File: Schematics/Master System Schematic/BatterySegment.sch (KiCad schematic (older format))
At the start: 148 parts

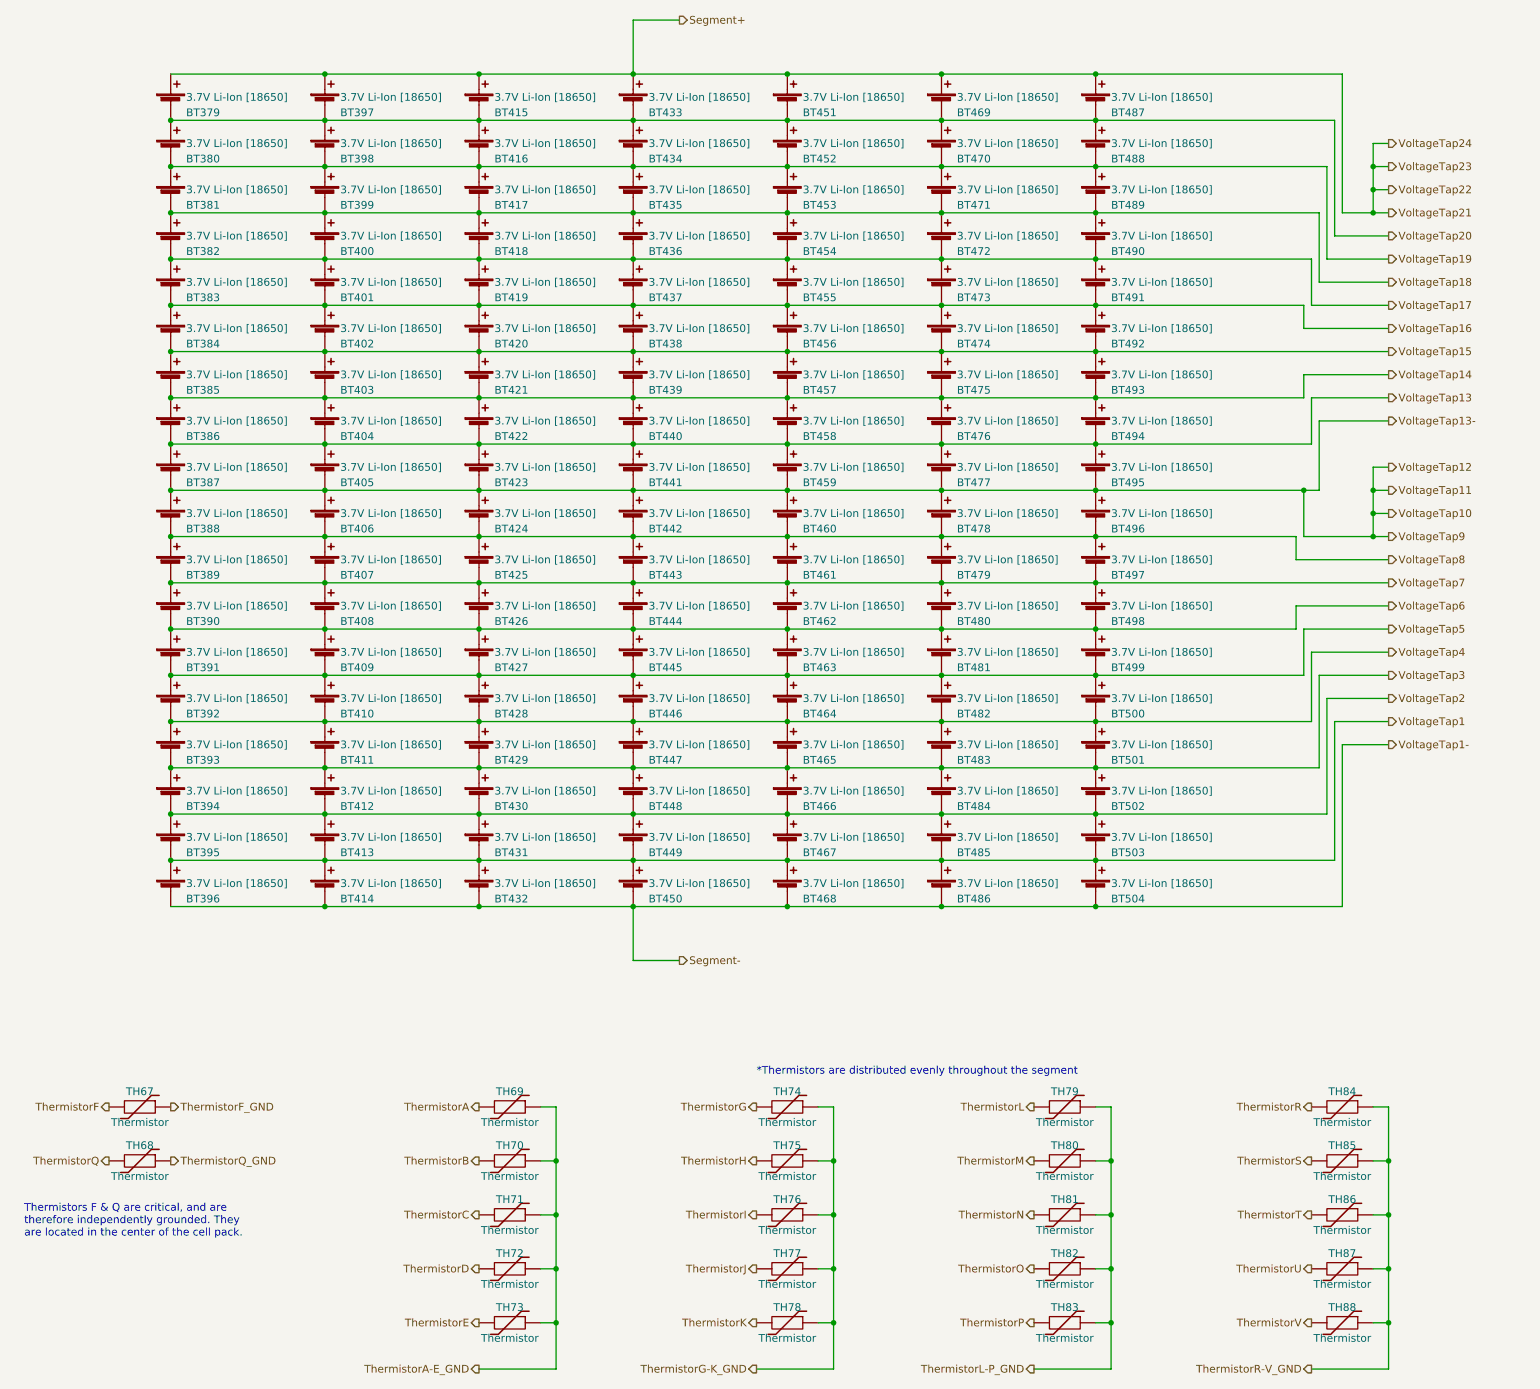
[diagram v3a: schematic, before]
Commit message: Had to refactor all IDs
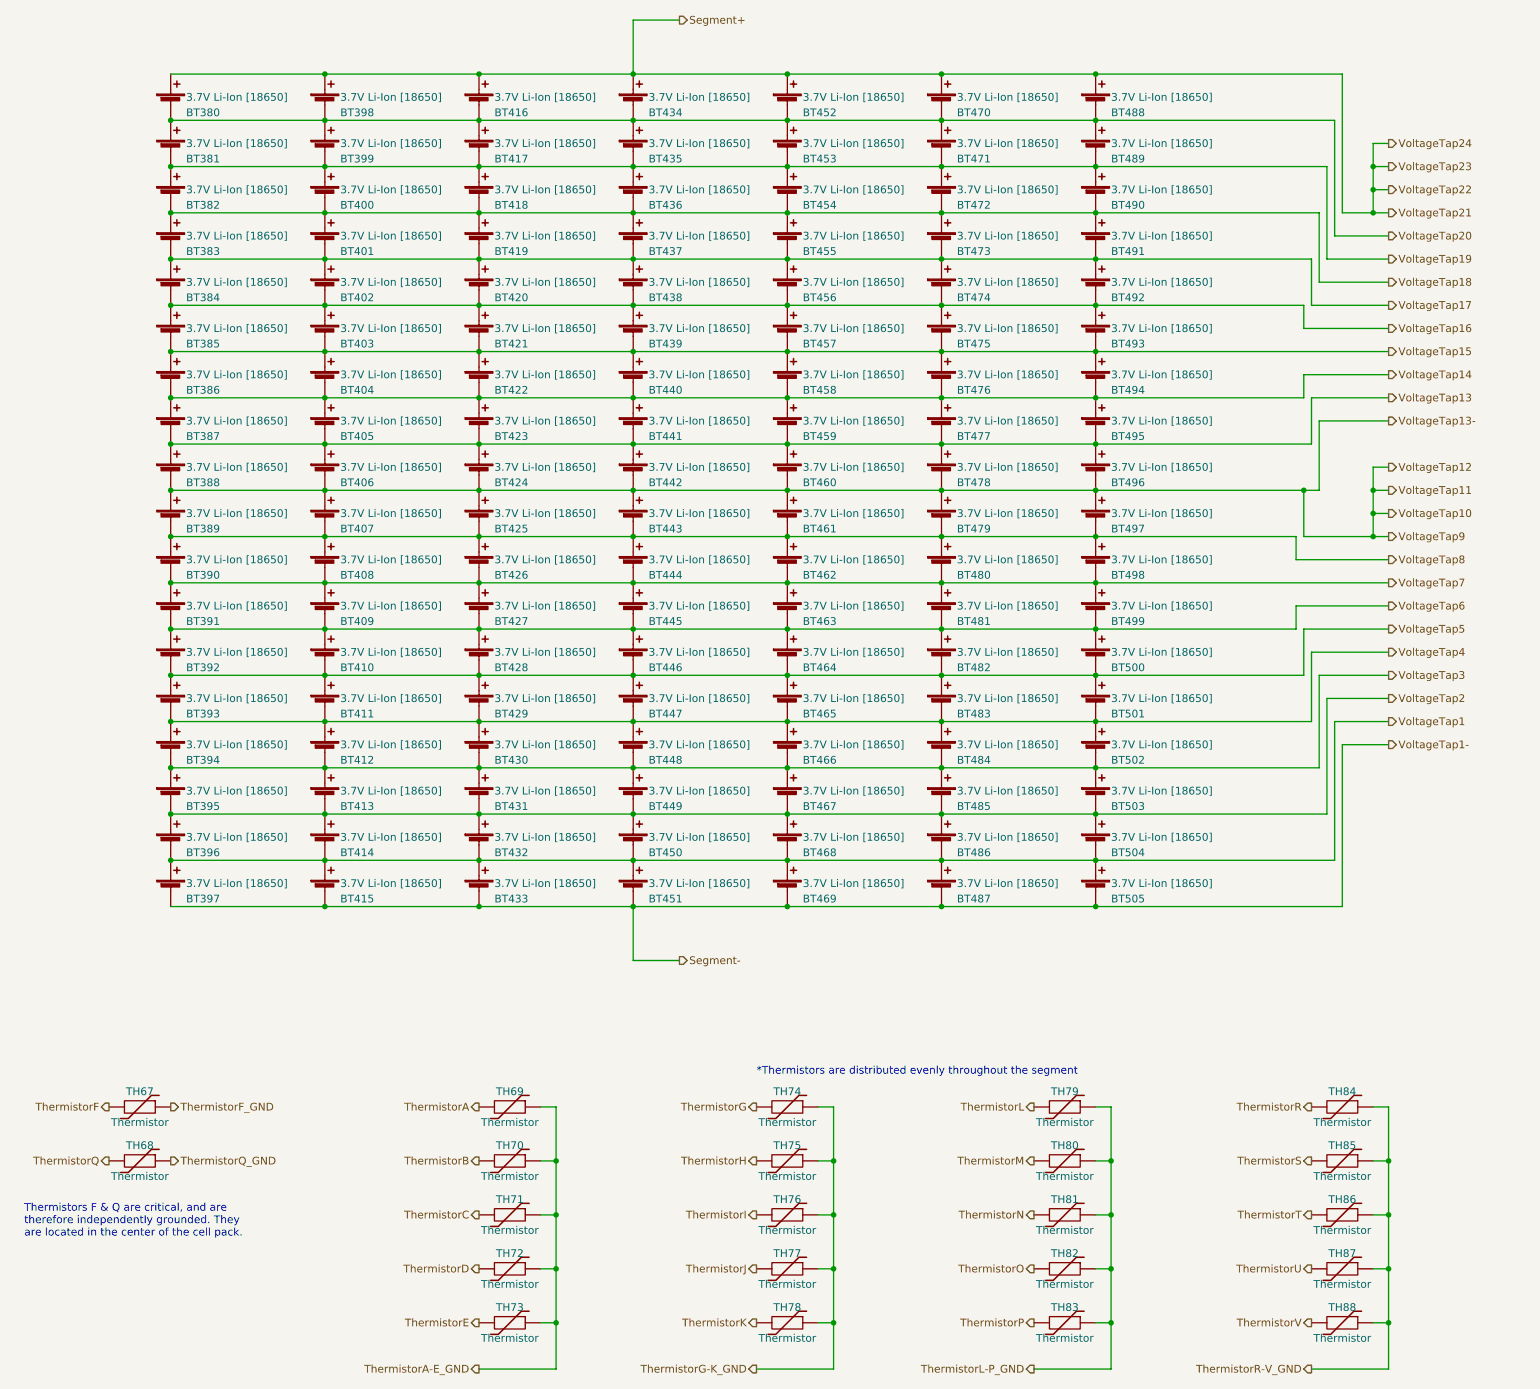
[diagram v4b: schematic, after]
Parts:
- renumbered BT15 to BT10, BT16 to BT11, BT7 to BT110, BT110 to BT111, BT111 to BT112, BT112 to BT113, BT113 to BT114, BT114 to BT115, BT115 to BT116, BT116 to BT117, BT117 to BT118, BT118 to BT119, BT17 to BT12, BT119 to BT120, BT120 to BT121, BT121 to BT122, BT122 to BT123, BT123 to BT124, BT124 to BT125, BT125 to BT126, BT126 to BT127, BT18 to BT13, BT19 to BT14, BT20 to BT15, BT21 to BT16, BT22 to BT17, BT23 to BT18, BT24 to BT19, BT1 to BT2, BT2 to BT20, BT25 to BT21, BT26 to BT22, BT27 to BT23, BT28 to BT24, BT29 to BT25, BT30 to BT26, BT31 to BT27, BT32 to BT28, BT33 to BT29, BT8 to BT3, BT34 to BT30, BT35 to BT31, BT36 to BT32, BT37 to BT33, BT38 to BT34, BT39 to BT35, BT40 to BT36, BT41 to BT37, BT3 to BT38, BT42 to BT39, BT9 to BT4, BT43 to BT40, BT44 to BT41, BT45 to BT42, BT46 to BT43, BT47 to BT44, BT48 to BT45, BT49 to BT46, BT50 to BT47, BT51 to BT48, BT52 to BT49, BT10 to BT5, BT53 to BT50, BT54 to BT51, BT55 to BT52, BT56 to BT53, BT57 to BT54, BT58 to BT55, BT4 to BT56, BT59 to BT57, BT60 to BT58, BT61 to BT59, BT11 to BT6, BT62 to BT60, BT63 to BT61, BT64 to BT62, BT65 to BT63, BT66 to BT64, BT67 to BT65, BT68 to BT66, BT69 to BT67, BT70 to BT68, BT71 to BT69, BT12 to BT7, BT72 to BT70, BT73 to BT71, BT74 to BT72, BT75 to BT73, BT5 to BT74, BT76 to BT75, BT77 to BT76, BT78 to BT77, BT79 to BT78, BT80 to BT79, BT13 to BT8, BT81 to BT80, BT82 to BT81, BT83 to BT82, BT84 to BT83, BT85 to BT84, BT86 to BT85, BT87 to BT86, BT88 to BT87, BT89 to BT88, BT90 to BT89, BT14 to BT9, BT91 to BT90, BT92 to BT91, BT6 to BT92, TH6 to TH1, TH9 to TH10, TH10 to TH11, TH11 to TH12, TH12 to TH13, TH13 to TH14, TH14 to TH15, TH15 to TH16, TH16 to TH17, TH17 to TH2, TH1 to TH3, TH2 to TH4, TH3 to TH5, TH4 to TH6, TH5 to TH7, TH7 to TH8, TH8 to TH9

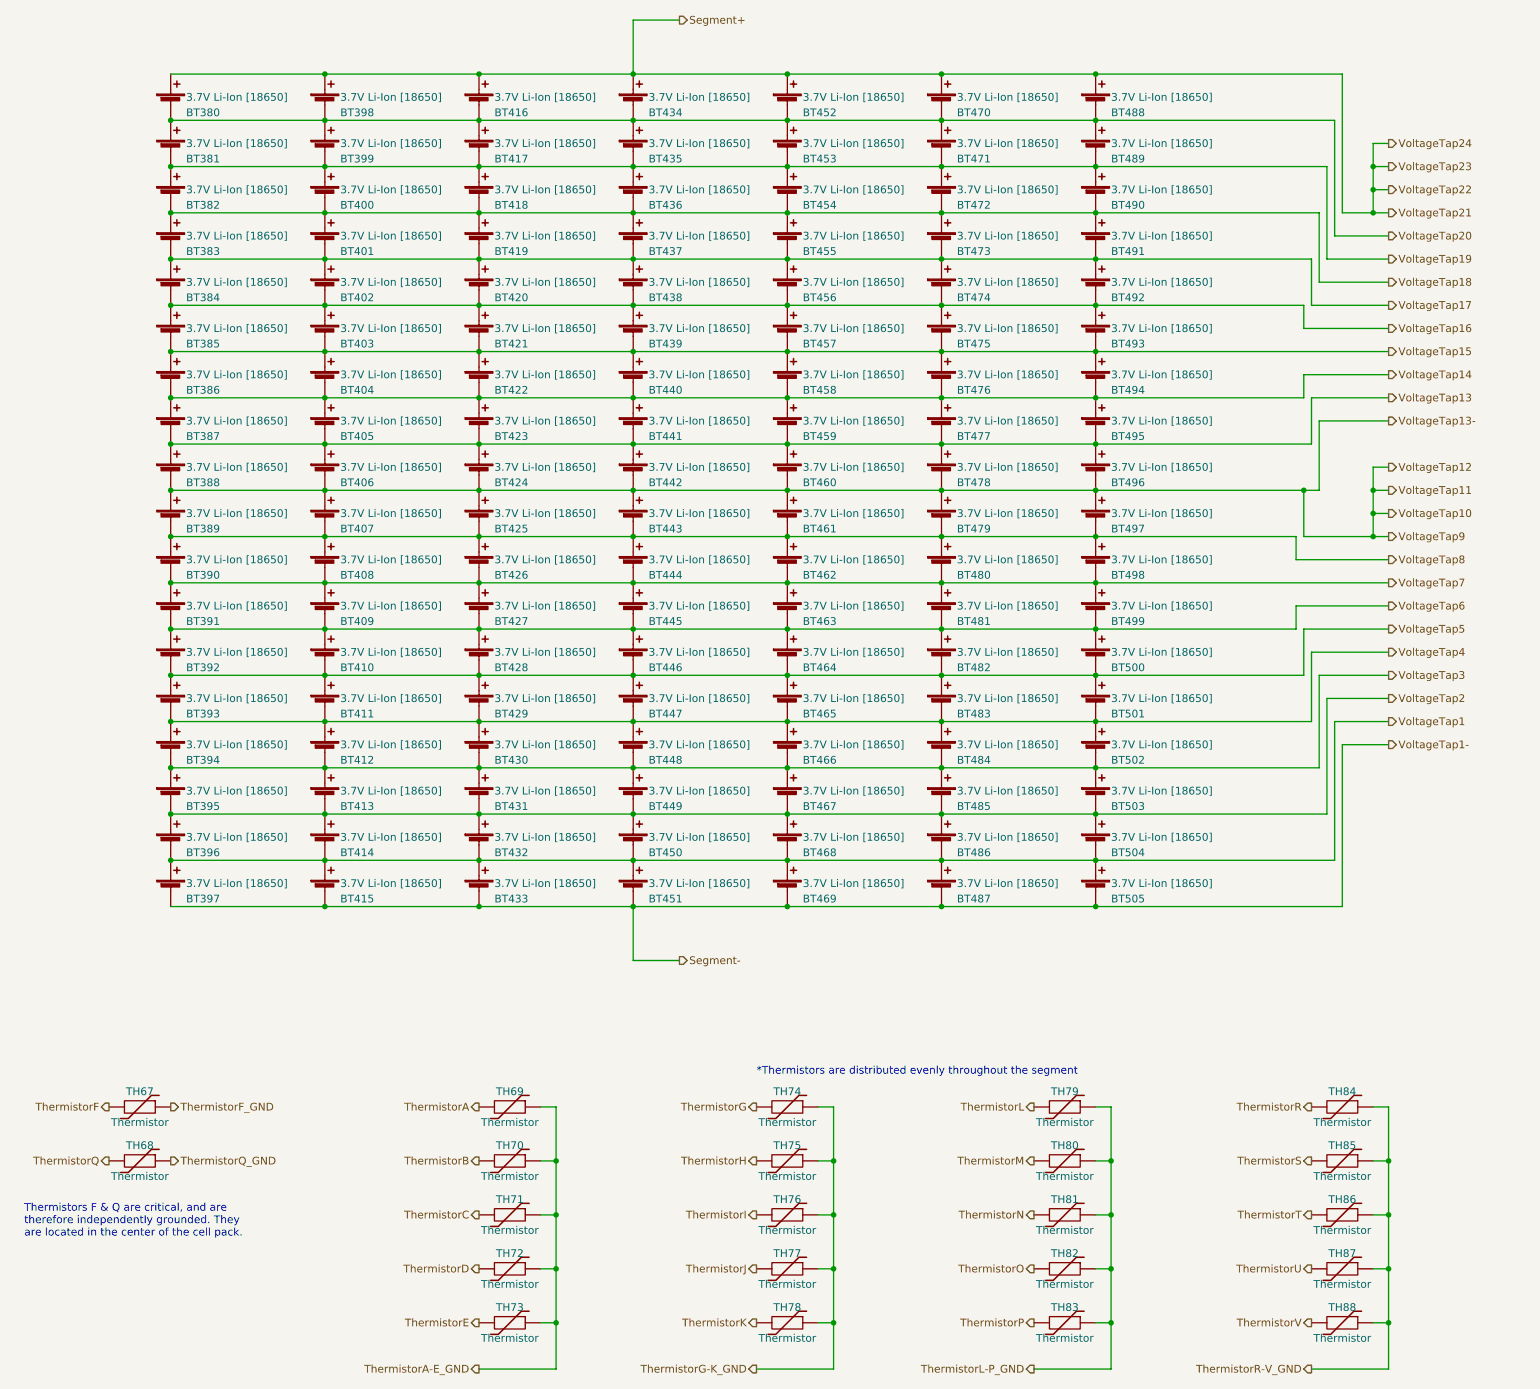
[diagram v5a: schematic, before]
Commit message: Fixed Segment tap wiring
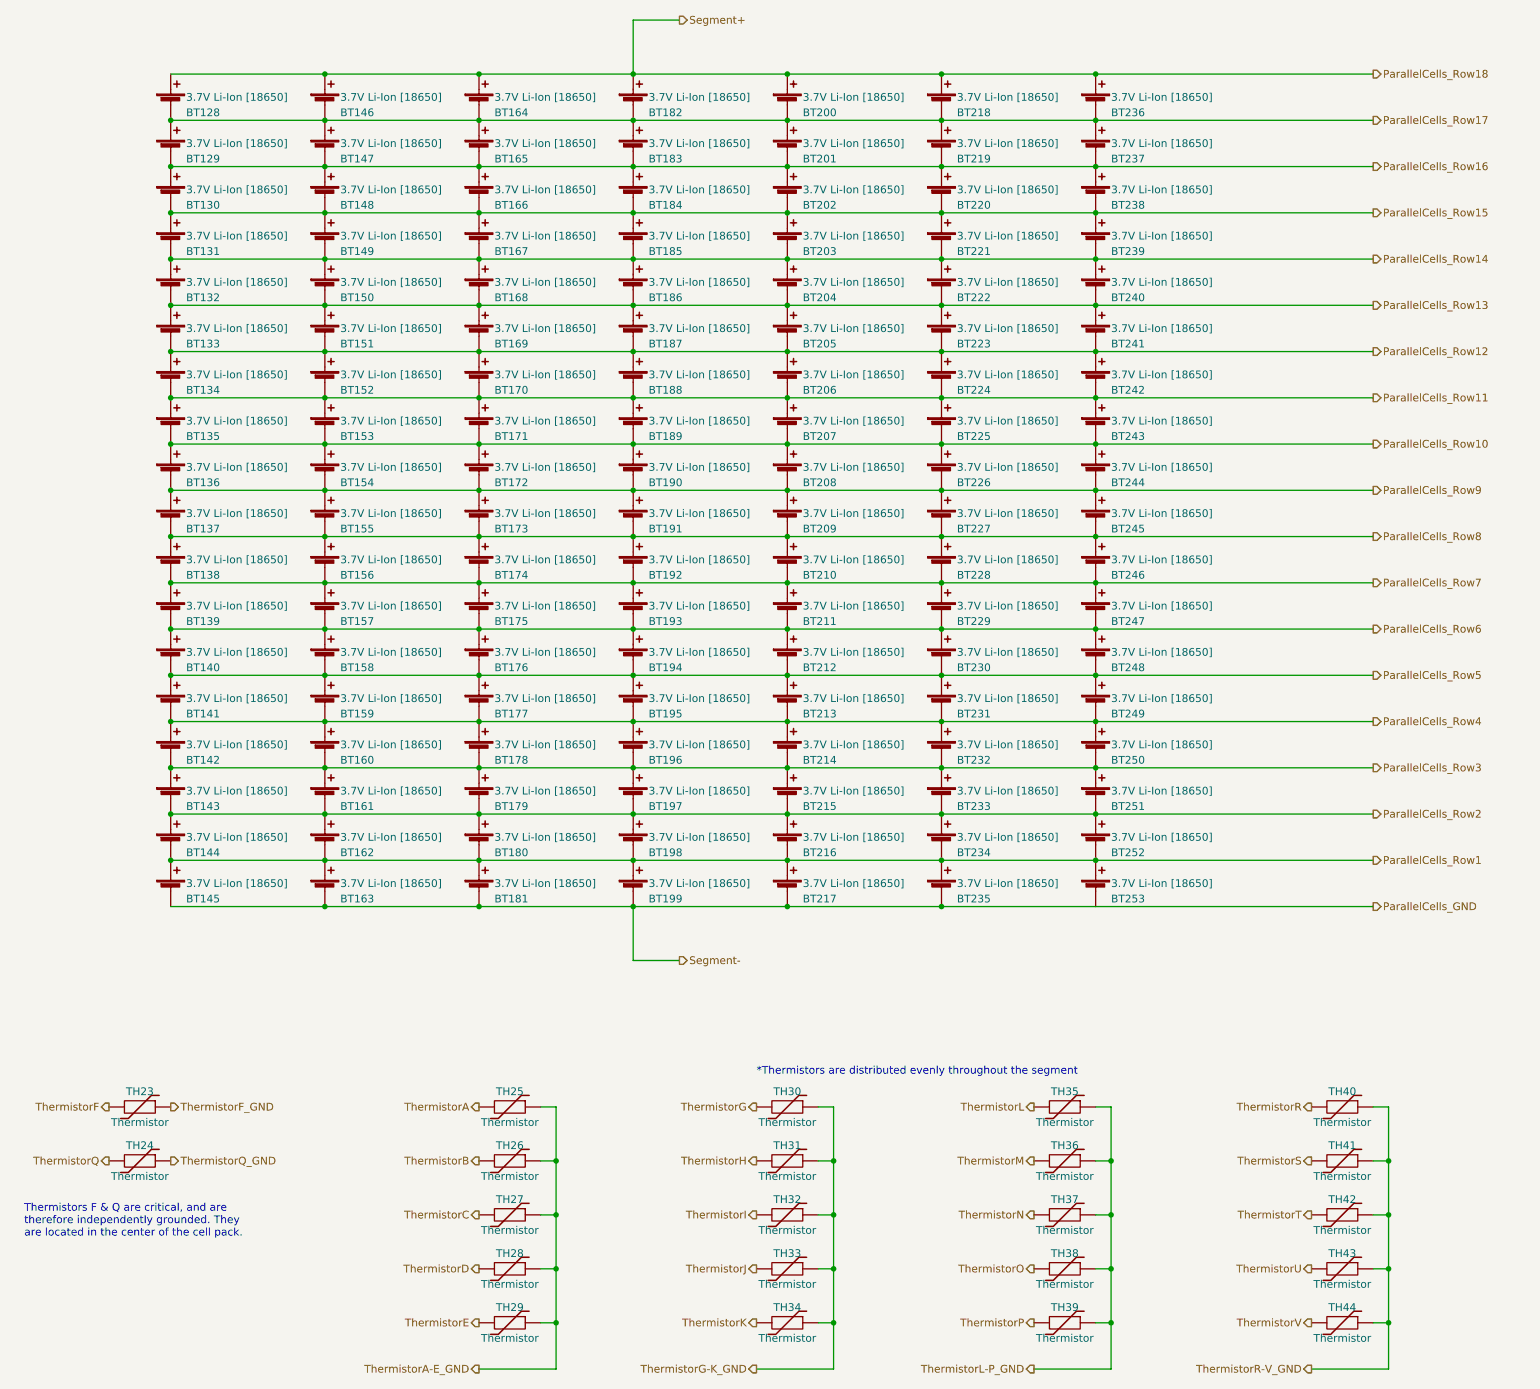
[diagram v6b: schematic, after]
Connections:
- net Segment+ renamed ParallelCells_Row18
- net Segment- renamed ParallelCells_GND
- net VoltageTap1 renamed ParallelCells_Row1
- net VoltageTap10 renamed ParallelCells_Row9
- net VoltageTap13 renamed ParallelCells_Row10
- net VoltageTap14 renamed ParallelCells_Row11
- net VoltageTap15 renamed ParallelCells_Row12
- net VoltageTap16 renamed ParallelCells_Row13
- net VoltageTap17 renamed ParallelCells_Row14
- net VoltageTap18 renamed ParallelCells_Row15
- net VoltageTap19 renamed ParallelCells_Row16
- net VoltageTap2 renamed ParallelCells_Row2
- net VoltageTap20 renamed ParallelCells_Row17
- net VoltageTap3 renamed ParallelCells_Row3
- net VoltageTap4 renamed ParallelCells_Row4
- net VoltageTap5 renamed ParallelCells_Row5
- net VoltageTap6 renamed ParallelCells_Row6
- net VoltageTap7 renamed ParallelCells_Row7
- net VoltageTap8 renamed ParallelCells_Row8

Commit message: Fixed annotations and date
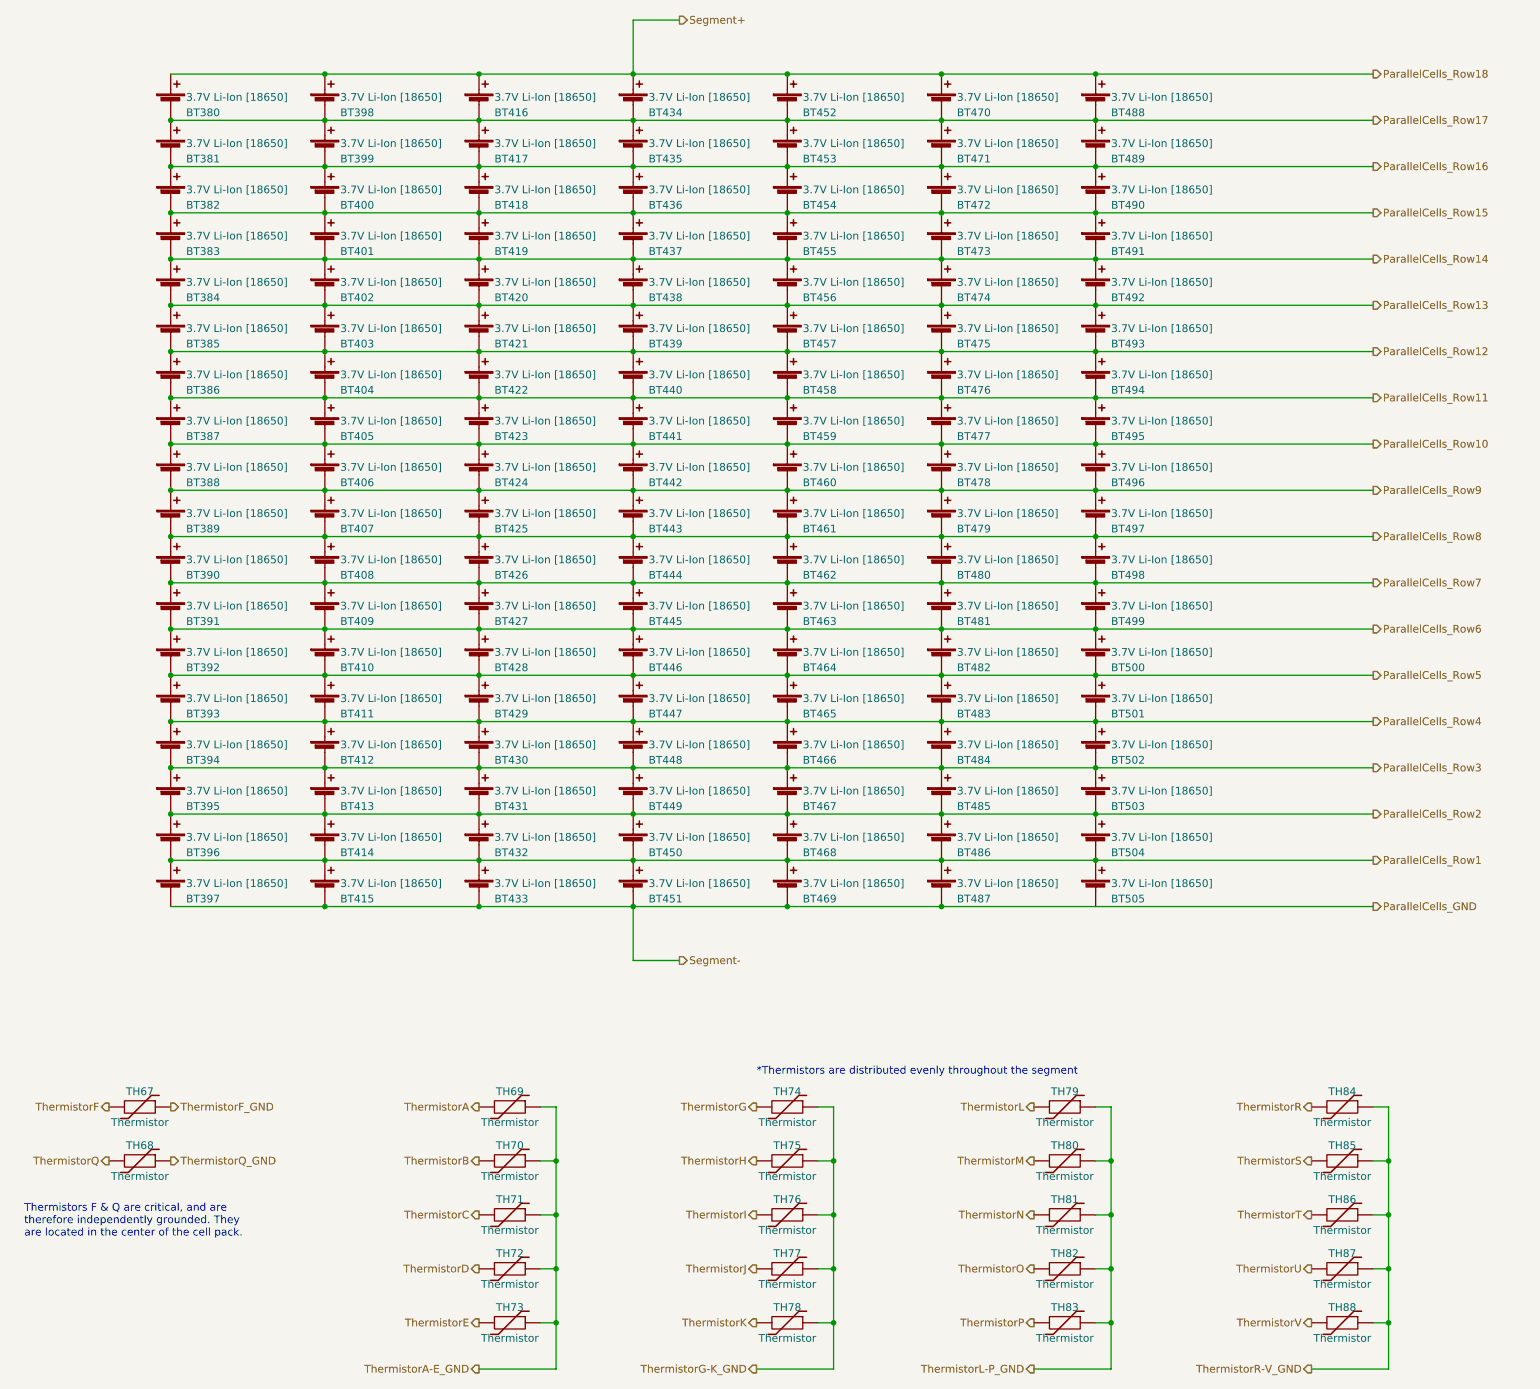
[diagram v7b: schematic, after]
